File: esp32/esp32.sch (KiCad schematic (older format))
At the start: 58 parts, among them IC1 KF33BDT-TR, J1 USB_C, J2 Conn_01x26, J3 Conn_01x26, Q1 FDN306P, Q2 8205A, Q3 BC817, Q4 BC817, SW1 Reset, SW2 Boot, U1 CH340G, U2 AP5056, U3 DW01A, X1 12 MHz

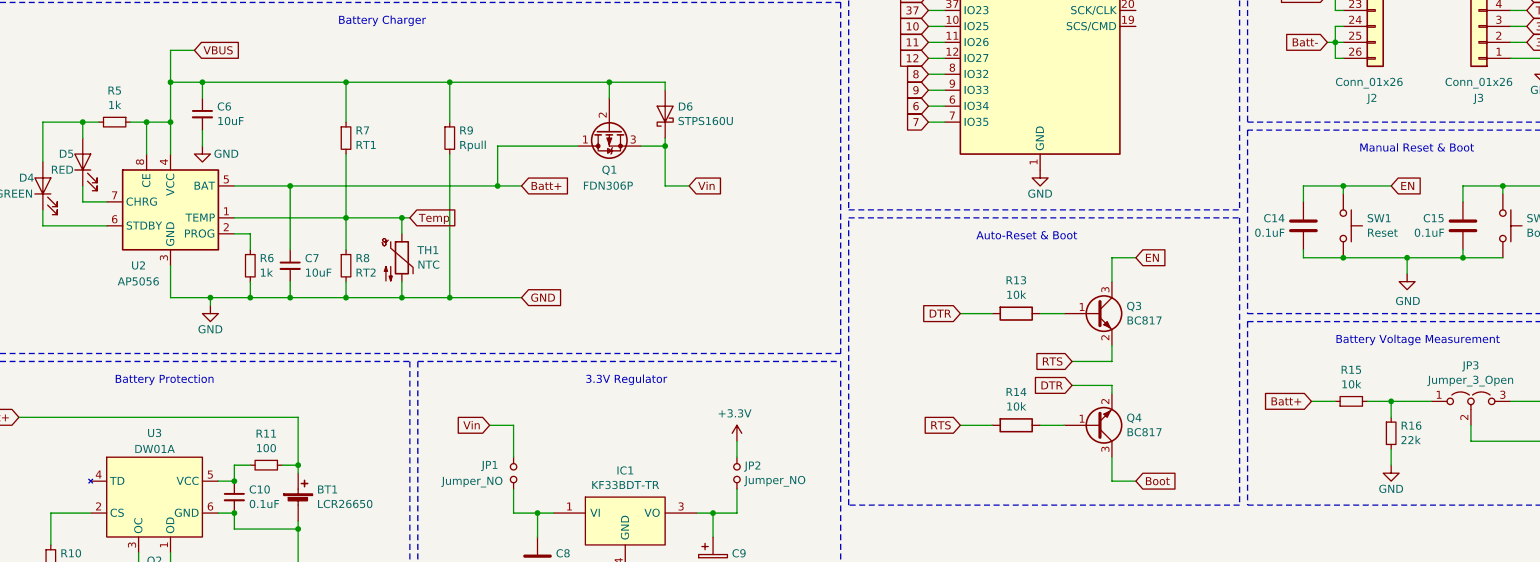
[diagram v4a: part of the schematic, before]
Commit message: Agregar simulaciones de sensores
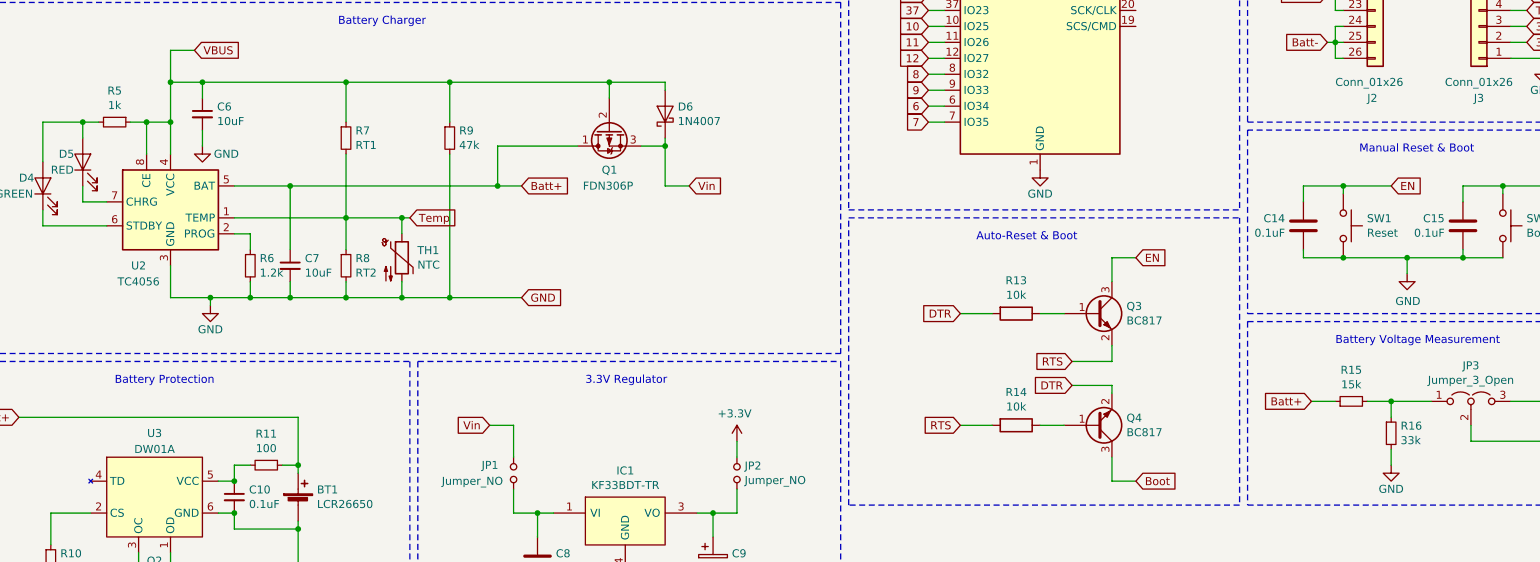
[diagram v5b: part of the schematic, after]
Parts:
- D6: value STPS160U -> 1N4007
- R15: value 10k -> 15k
- R16: value 22k -> 33k
- R6: value 1k -> 1.2k
- R9: value Rpull -> 47k
- U2: value AP5056 -> TC4056
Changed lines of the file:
@@
 P 2150 4550
 F 0 "U2" H 1950 4150 50  0000 C CNN
-F 1 "AP5056" H 1950 4050 50  0000 C CNN
+F 1 "TC4056" H 1950 4050 50  0000 C CNN
 F 2 "Package_SO:SOIC-8_3.9x4.9mm_P1.27mm" H 2000 5300 50  0001 C CNN
 F 3 "http://file.yizimg.com/328625/2012112613030098.pdf" H 2050 4750 50  0001 C CNN
@@
 P 2650 4950
 F 0 "R6" H 2709 4996 50  0000 L CNN
-F 1 "1k" H 2709 4905 50  0000 L CNN
+F 1 "1.2k" H 2709 4905 50  0000 L CNN
 F 2 "Resistor_SMD:R_0805_2012Metric_Pad1.15x1.40mm_HandSolder" H 2650 4950 50  0001 C CNN
 F 3 "~" H 2650 4950 50  0001 C CNN
@@
 P 5250 4000
 F 0 "D6" V 5296 3921 50  0000 R CNN
-F 1 "STPS160U" V 5205 3921 50  0000 R CNN
+F 1 "1N4007" V 5205 3921 50  0000 R CNN
 F 2 "Diode_SMD:D_SMB_Handsoldering" H 5250 4000 50  0001 C CNN
 F 3 "~" H 5250 4000 50  0001 C CNN
@@
 P 3900 4150
 F 0 "R9" H 3959 4196 50  0000 L CNN
-F 1 "Rpull" H 3959 4105 50  0000 L CNN
+F 1 "47k" H 3959 4105 50  0000 L CNN
 F 2 "Resistor_SMD:R_0805_2012Metric_Pad1.15x1.40mm_HandSolder" H 3900 4150 50  0001 C CNN
 F 3 "~" H 3900 4150 50  0001 C CNN
@@
 P 9800 6000
 F 0 "R16" H 9859 6046 50  0000 L CNN
-F 1 "22k" H 9859 5955 50  0000 L CNN
+F 1 "33k" H 9859 5955 50  0000 L CNN
 F 2 "Resistor_SMD:R_0805_2012Metric_Pad1.15x1.40mm_HandSolder" H 9800 6000 50  0001 C CNN
 F 3 "~" H 9800 6000 50  0001 C CNN
@@
 P 9550 5800
 F 0 "R15" V 9746 5800 50  0000 C CNN
-F 1 "10k" V 9655 5800 50  0000 C CNN
+F 1 "15k" V 9655 5800 50  0000 C CNN
 F 2 "Resistor_SMD:R_0805_2012Metric_Pad1.15x1.40mm_HandSolder" H 9550 5800 50  0001 C CNN
 F 3 "~" H 9550 5800 50  0001 C CNN
